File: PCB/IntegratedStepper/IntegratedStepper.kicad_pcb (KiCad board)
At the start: 4 copper layers, 57 x 42.5 mm, 81 parts, among them CN1 PJ-35825, CN2 PJ-35825, IC2 SN65HVD230DR, IC3 LMR38020FSQDDARQ1, IC4 DRV8243HQRXYRQ1, IC5 DRV8243HQRXYRQ1, J3 Screw_Terminal_01x02, J4 Screw_Terminal_01x02, J5 Conn_01x05_Socket, Q1 SS8050-G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

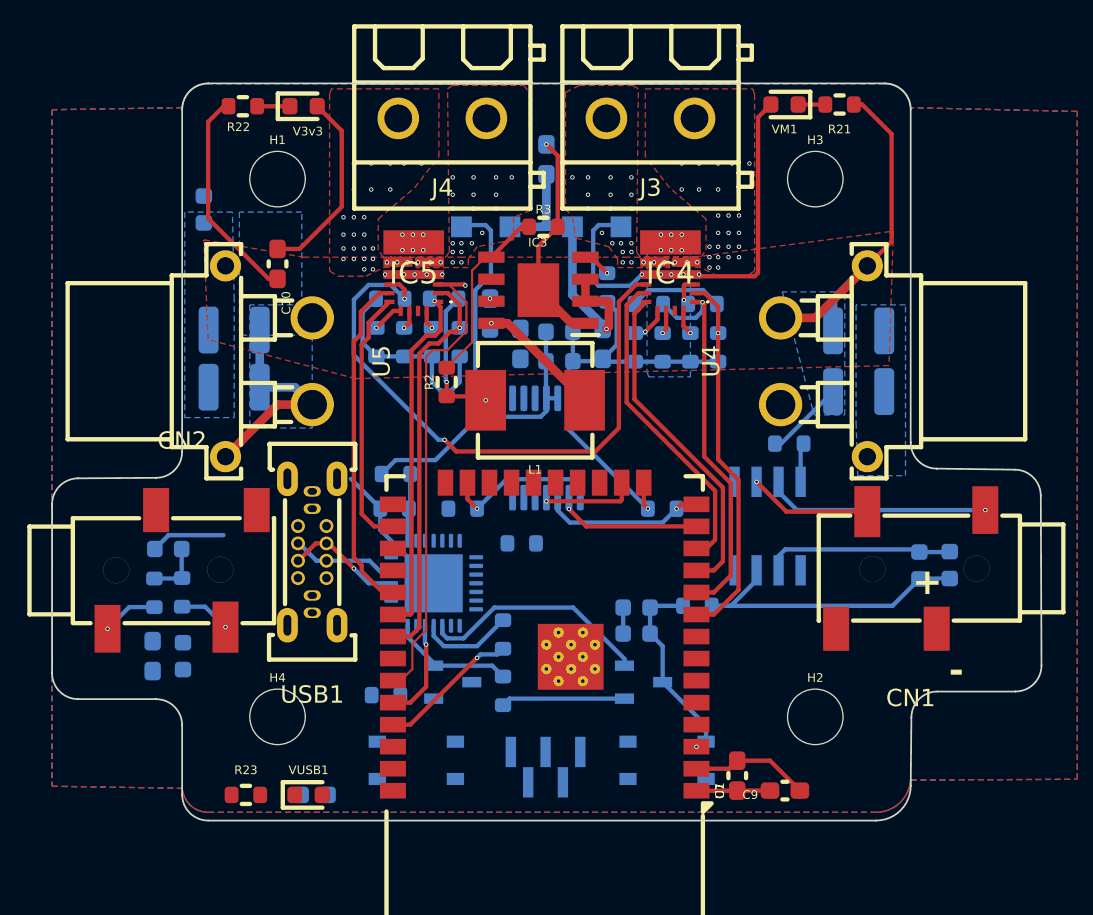
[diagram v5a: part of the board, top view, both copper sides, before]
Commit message: finalize layout w/ thermals
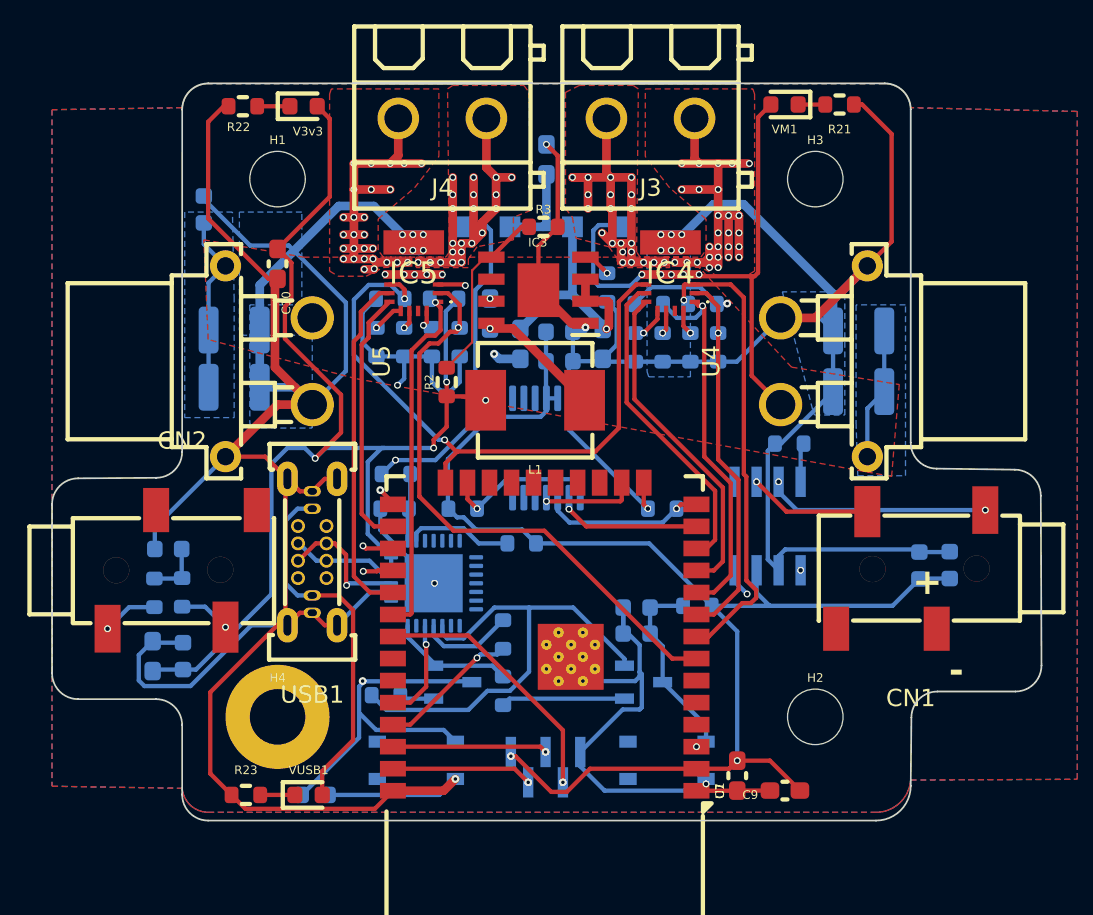
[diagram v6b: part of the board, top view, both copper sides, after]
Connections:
- U1 pad 31: IPROPI_2 -> /ESP32_MCU/ENC_IND
- U1 pad 33: /DRV8844/NSLEEP -> /ESP32_MCU/I2C_SCL
- U1 pad 36: /ESP32_MCU/I2C_SCL -> /ESP32_MCU/ENC+
- U1 pad 37: unconnected-(U1-IO23-Pad37) -> /ESP32_MCU/ENC-
- U1 pad 6: unconnected-(U1-IO34-Pad6) -> /ESP32_MCU/I2C_SDA
- U1 pad 7: /ESP32_MCU/ENC_IND -> IPROPI_2
- U1 pad 8: unconnected-(U1-IO32-Pad8) -> /DRV8844/NSLEEP
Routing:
- net GND: track 132.6 -> 353.6 mm, vias 14 -> 20
- net 3V3_VCC: track 59.1 -> 171.7 mm, vias 2 -> 7
- net /3V3_VReg/VM: track 21.4 -> 110.9 mm
- net CANL: track 16.1 -> 60.7 mm, vias 2 -> 3
- net CANH: track 10.1 -> 50.9 mm
- net IO0: track 0.00 -> 33.6 mm, vias 0 -> 2
- net /CAN_Transciever/CAN_TX: track 0.00 -> 27.6 mm, vias 0 -> 2
- net /3V3_VReg/V_USB: track 19.9 -> 47.2 mm, vias 0 -> 1
- net /CAN_Transciever/CAN_RX: track 0.00 -> 26.1 mm, vias 0 -> 2
- net /DRV8844/OUT1: track 0.00 -> 23.8 mm
- net /DRV8844/OUT2: track 0.00 -> 23.0 mm, vias 3 -> 27
- net /DRV8844/OUT3: track 0.00 -> 21.6 mm, vias 51 -> 27
- net /DRV8844/OUT4: track 0.00 -> 21.2 mm
- net /ESP32_MCU/ENC_IND: track 0.00 -> 15.4 mm, vias 0 -> 1
- net RTS: track 13.4 -> 27.5 mm
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- added copper zone on F.Cu, net /DRV8844/OUT1
- added copper zone on In1.Cu, net /DRV8844/OUT1
- added copper zone on In2.Cu, net /DRV8844/OUT1
- added copper zone on F.Cu, net /DRV8844/OUT2
- added copper zone on In1.Cu, net /DRV8844/OUT2
- added copper zone on In2.Cu, net /DRV8844/OUT2
- added copper zone on In1.Cu, net /DRV8844/OUT3
- added copper zone on In2.Cu, net /DRV8844/OUT3
- added copper zone on In1.Cu, net /DRV8844/OUT4
- added copper zone on In2.Cu, net /DRV8844/OUT4

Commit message: Update final layout, replace CAN w/ JST
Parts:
- removed CN1, CN2: PJ-35825, easyeda2kicad:AUDIO-SMD_PJ-35825
- added U6: SM04B-GHS-TB(LF)(SN), easyeda2kicad:CONN-SMD_4P-P1.25_SM04B-GHS-TB-LF-SN, F.Cu at (103.2, 127.5)
- added U7: SM04B-GHS-TB(LF)(SN), easyeda2kicad:CONN-SMD_4P-P1.25_SM04B-GHS-TB-LF-SN, F.Cu at (138.8, 127.5)
- R1, R13, R14: value 10k -> 8.2k
- R15, R16, R_DRV1, R_SLEEP1, R_nFAULT_1, R_nFAULT_2: value 2k -> 8.2k
- R21: value 10K -> 8.2k
- moved C13 4.73 mm to (137.8, 127.8)
- moved C18 4.73 mm to (139.5, 127.8)
- moved C15 4.59 mm to (102.8, 124.0)
- moved C19 4.59 mm to (103.6, 130.1)
- moved C8 4.59 mm to (101.9, 130.1)
- moved R7 4.59 mm to (103.6, 126.5)
- moved R8 4.59 mm to (102.0, 126.5)
- moved D2 0.18 mm to (117.5, 108.1)
- moved D1 0.17 mm to (123.9, 108.1)
- moved VUSB1 0.15 mm to (107.3, 140.8)
- moved R23 0.08 mm to (103.7, 140.9)
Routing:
- net CANL: track 60.7 -> 48.5 mm, vias 3 -> 2
- net 3V3_VCC: track 171.7 -> 162.9 mm
- net CANH: track 50.9 -> 44.1 mm
- net GND: track 353.6 -> 357.8 mm
- net /DRV8844/OUT1: track 23.8 -> 24.3 mm, vias 21 -> 18
- net /DRV8844/OUT3: track 21.6 -> 21.2 mm, vias 27 -> 24
- net /DRV8844/OUT4: track 21.2 -> 21.5 mm, vias 21 -> 19
- net /DRV8844/OUT2: track 23.0 -> 22.8 mm, vias 27 -> 26
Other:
- board size 57 x 42.5 mm -> 42 x 42.5 mm
- board text added: "v2.0, 5/2024"
- board text removed: "v1.0, 3/2024"

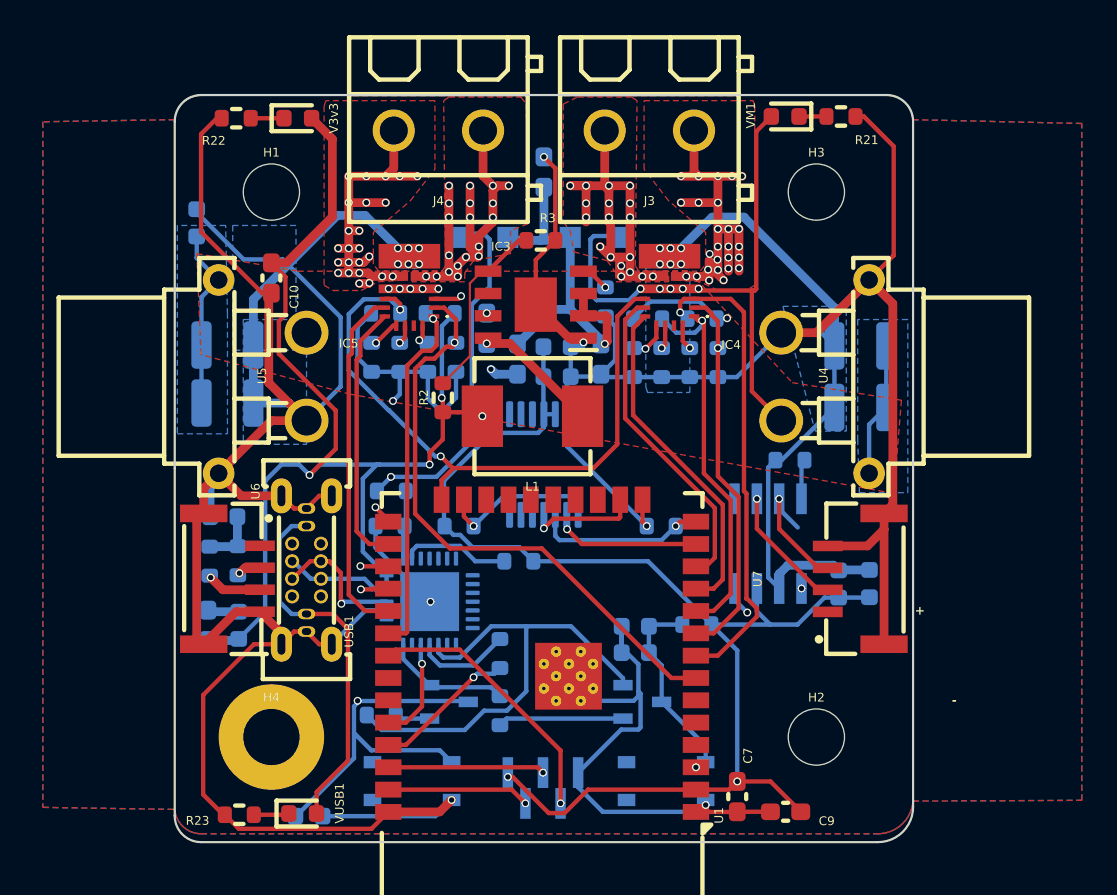
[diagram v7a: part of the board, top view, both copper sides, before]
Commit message: update new layout with DRV8245
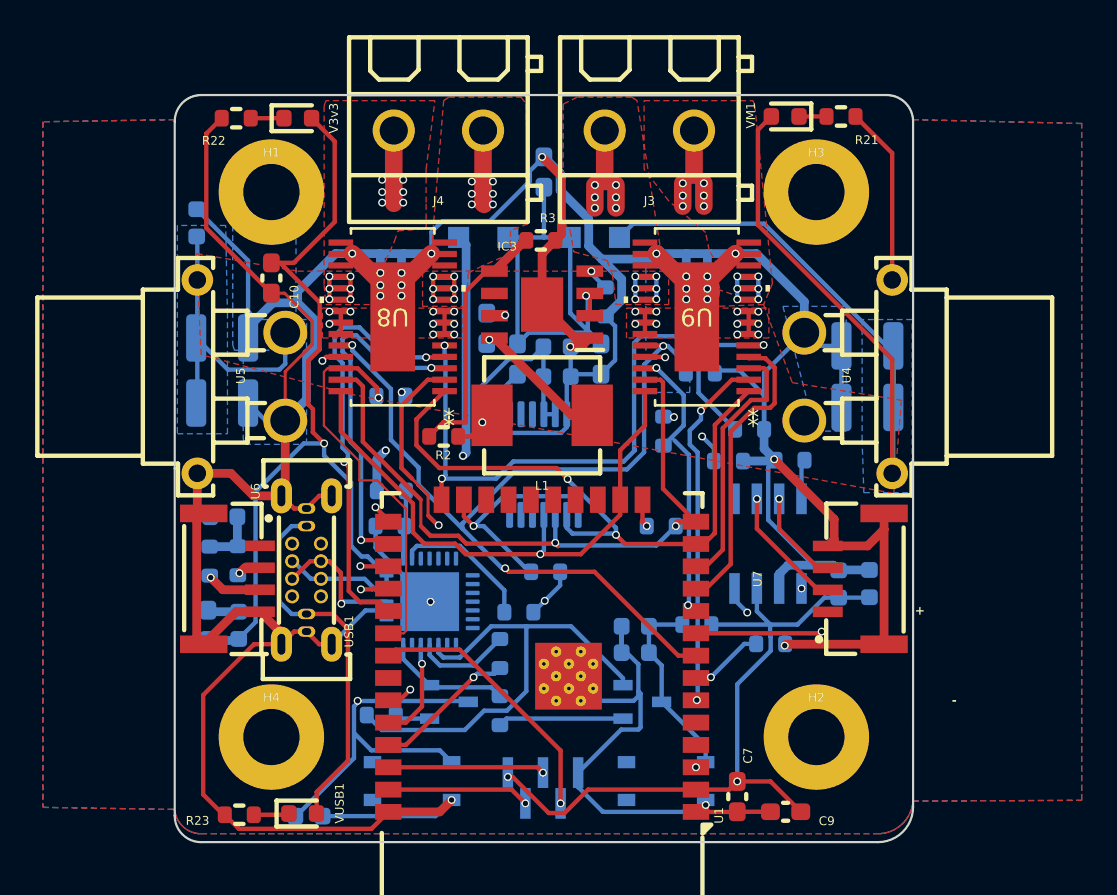
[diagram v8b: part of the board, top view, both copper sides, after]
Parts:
- removed IC4, IC5: DRV8243HQRXYRQ1, SamacSys_Parts:DRV8243HQRXYRQ1
- removed R_DIAG1, R_DIAG2, R_MODE1, R_MODE2, R_SLEEP1, R_SR1, R_SR2: 8.2k, Resistor_SMD:R_0603_1608Metric
- added R_nSLEEP1: 8.2k, Resistor_SMD:R_0603_1608Metric, B.Cu at (129.9, 115.8)
- added U8: PDRV8245SPWPQ1, PDRV8245SPWPQ1:U_PWP0028R_TEX, F.Cu at (112.4, 112.6)
- added U9: PDRV8245SPWPQ1, PDRV8245SPWPQ1:U_PWP0028R_TEX, F.Cu at (129.7, 112.6)
- moved R_IPROP2 24.2 mm to (133.9, 131.2), turned to 0 degrees
- moved R_DRV1 21.7 mm to (132.7, 119.0), turned to 180 degrees
- moved R_nFAULT_1 6.46 mm to (127.8, 119.1), turned to 90 degrees
- moved R_IPROP1 5.63 mm to (131.5, 120.8), turned to 0 degrees
- moved R15 5.57 mm to (121.1, 127.1), turned to 0 degrees
- moved R_nFAULT_2 5.47 mm to (112.3, 117.1)
- moved R12 2.90 mm to (119.6, 129.4)
- moved R2 2.20 mm to (115.3, 119.4), turned to 180 degrees
- moved U4 1.31 mm to (138.3, 116.0)
- moved U5 1.21 mm to (103.8, 116.0)
- moved L1 0.55 mm to (120.9, 118.2)
- moved C27 0.50 mm to (102.7, 113.8)
- moved C23 0.40 mm to (139.4, 114.2)
- moved C24 0.40 mm to (139.4, 117.8)
- moved IC3 0.36 mm to (120.9, 111.9)
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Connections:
- net /DRV8844/DRVOFF renamed /DRV8245/DRVOFF
- net /DRV8844/NFAULT_1 renamed /DRV8245/NFAULT_1
- net /DRV8844/NFAULT_2 renamed /DRV8245/NFAULT_2
- net /ESP32_MCU/M_MISO renamed /DRV8245/M_MISO
- net /ESP32_MCU/M_MOSI renamed /DRV8245/M_MOSI
- net /ESP32_MCU/M_SCLK renamed /DRV8245/M_SCLK
- J3 pad 1: /DRV8844/OUT2 -> /DRV8245/OUT1
- J3 pad 2: /DRV8844/OUT1 -> /DRV8245/OUT2
- J4 pad 1: /DRV8844/OUT4 -> /DRV8245/OUT3
- J4 pad 2: /DRV8844/OUT3 -> /DRV8245/OUT4
- U1 pad 11: IN2 -> IN1
- U1 pad 12: IN1 -> IN2
- U1 pad 33: /ESP32_MCU/I2C_SCL -> /DRV8245/DRV2_CS
- U1 pad 6: /ESP32_MCU/I2C_SDA -> /DRV8245/DRV1_CS
- U1 pad 8: /DRV8844/NSLEEP -> /DRV8245/NSLEEP
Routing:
- net /DRV8245/NSLEEP: track 0.00 -> 51.4 mm, vias 0 -> 3
- net /DRV8844/NSLEEP: track 42.9 -> 0.00 mm, vias 2 -> 0
- net /DRV8245/M_MISO: track 9.73 -> 39.9 mm, vias 1 -> 2
- net /DRV8245/M_SCLK: track 7.68 -> 36.1 mm, vias 1 -> 2
- net /DRV8245/M_MOSI: track 5.60 -> 32.9 mm
- net /DRV8844/OUT1: track 24.3 -> 0.00 mm, vias 18 -> 0
- net /DRV8245/OUT1: track 0.00 -> 23.4 mm, vias 0 -> 12
- net /DRV8245/DRV2_CS: track 0.00 -> 22.8 mm, vias 0 -> 2
- net /DRV8844/OUT2: track 22.8 -> 0.00 mm, vias 26 -> 0
- net /DRV8245/OUT4: track 0.00 -> 22.2 mm, vias 0 -> 12
- net /DRV8245/OUT2: track 0.00 -> 21.6 mm, vias 0 -> 12
- net /DRV8844/OUT4: track 21.5 -> 0.00 mm, vias 19 -> 0
- net /DRV8844/OUT3: track 21.2 -> 0.00 mm, vias 24 -> 0
- net /DRV8245/OUT3: track 0.00 -> 21.0 mm, vias 0 -> 12
- net /DRV8245/DRV1_CS: track 0.00 -> 20.4 mm, vias 0 -> 2
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- added copper zone on F.Cu, net /DRV8245/OUT1
- added copper zone on In1.Cu, net /DRV8245/OUT1
- added copper zone on In2.Cu, net /DRV8245/OUT1
- added copper zone on F.Cu, net /DRV8245/OUT2
- added copper zone on In1.Cu, net /DRV8245/OUT2
- added copper zone on In2.Cu, net /DRV8245/OUT2
- added copper zone on F.Cu, net /DRV8245/OUT3
- added copper zone on In1.Cu, net /DRV8245/OUT3
- added copper zone on In2.Cu, net /DRV8245/OUT3
- added copper zone on F.Cu, net /DRV8245/OUT4
- added copper zone on In1.Cu, net /DRV8245/OUT4
- added copper zone on In2.Cu, net /DRV8245/OUT4
- added copper zone on In1.Cu, net GND
- removed copper zone on F.Cu, net /DRV8844/OUT1
- removed copper zone on In1.Cu, net /DRV8844/OUT1
- removed copper zone on In2.Cu, net /DRV8844/OUT1
- removed copper zone on F.Cu, net /DRV8844/OUT2
- removed copper zone on In1.Cu, net /DRV8844/OUT2
- removed copper zone on In2.Cu, net /DRV8844/OUT2
- removed copper zone on F.Cu, net /DRV8844/OUT3
- removed copper zone on In1.Cu, net /DRV8844/OUT3
- removed copper zone on In2.Cu, net /DRV8844/OUT3
- removed copper zone on F.Cu, net /DRV8844/OUT4
- removed copper zone on In1.Cu, net /DRV8844/OUT4
- removed copper zone on In2.Cu, net /DRV8844/OUT4
